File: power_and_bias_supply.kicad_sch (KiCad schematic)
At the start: 44 parts, among them Q501 2N7002, U501 MCP6L02x-xSN, U502 LM2733YMFX/NOPB, U503 TPS22944DCKR, X5 Conn_Coaxial

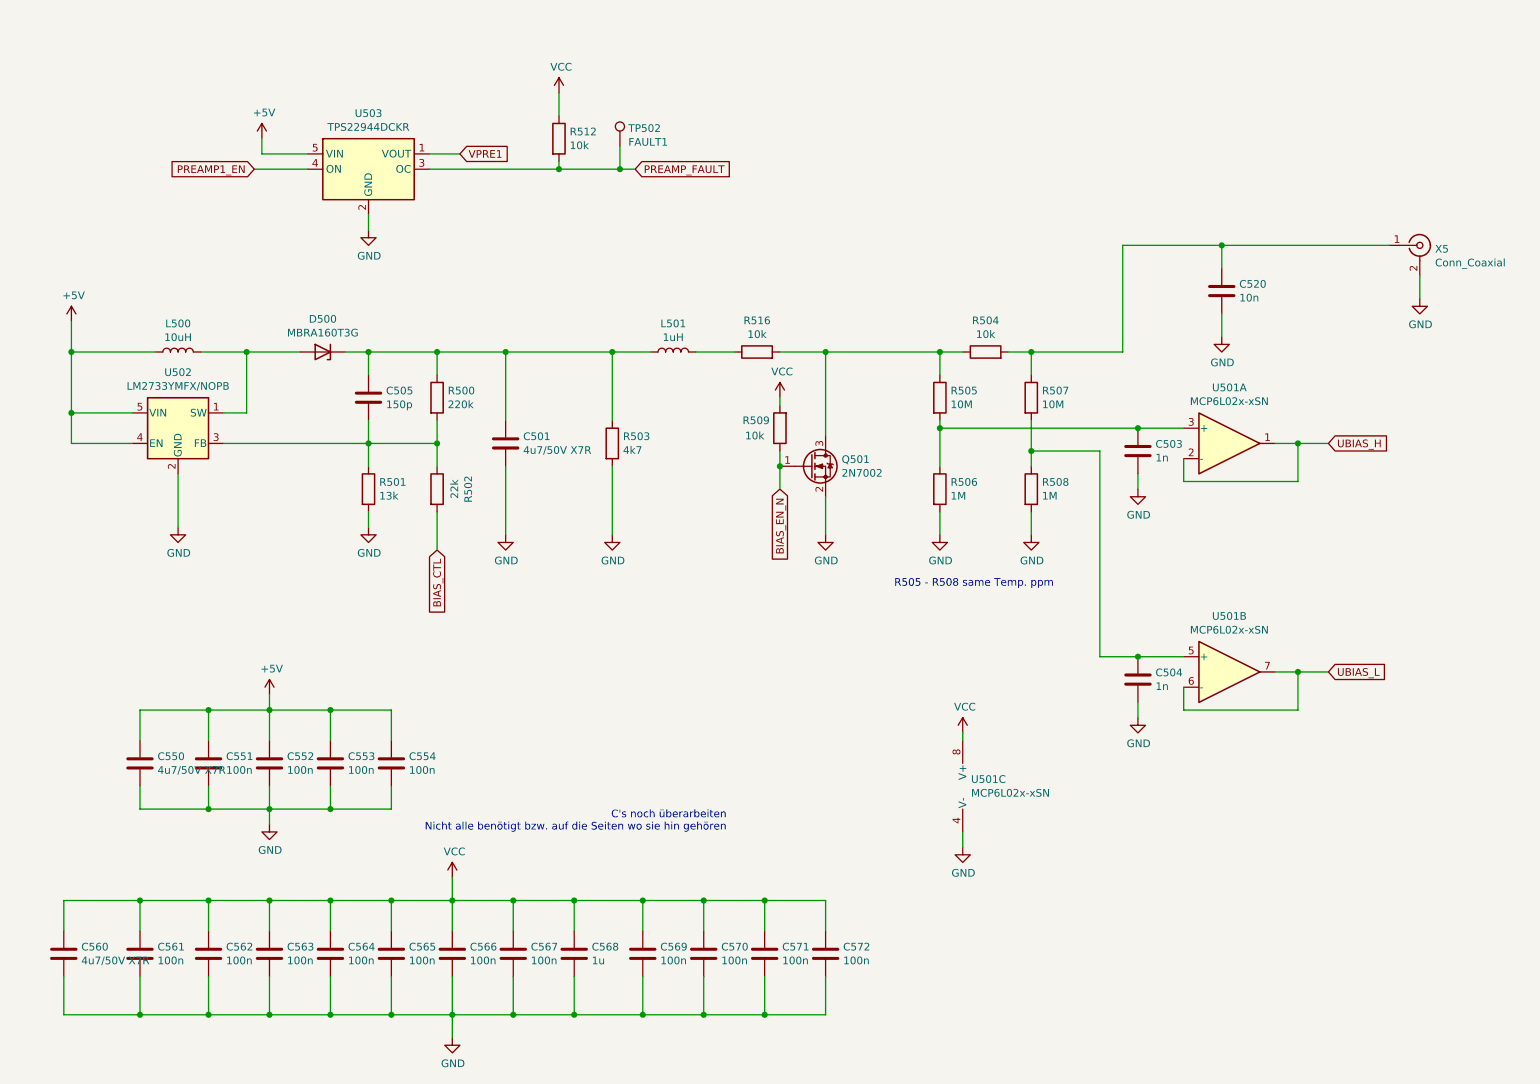
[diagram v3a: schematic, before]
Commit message: Footprints assigned. Testpoints added
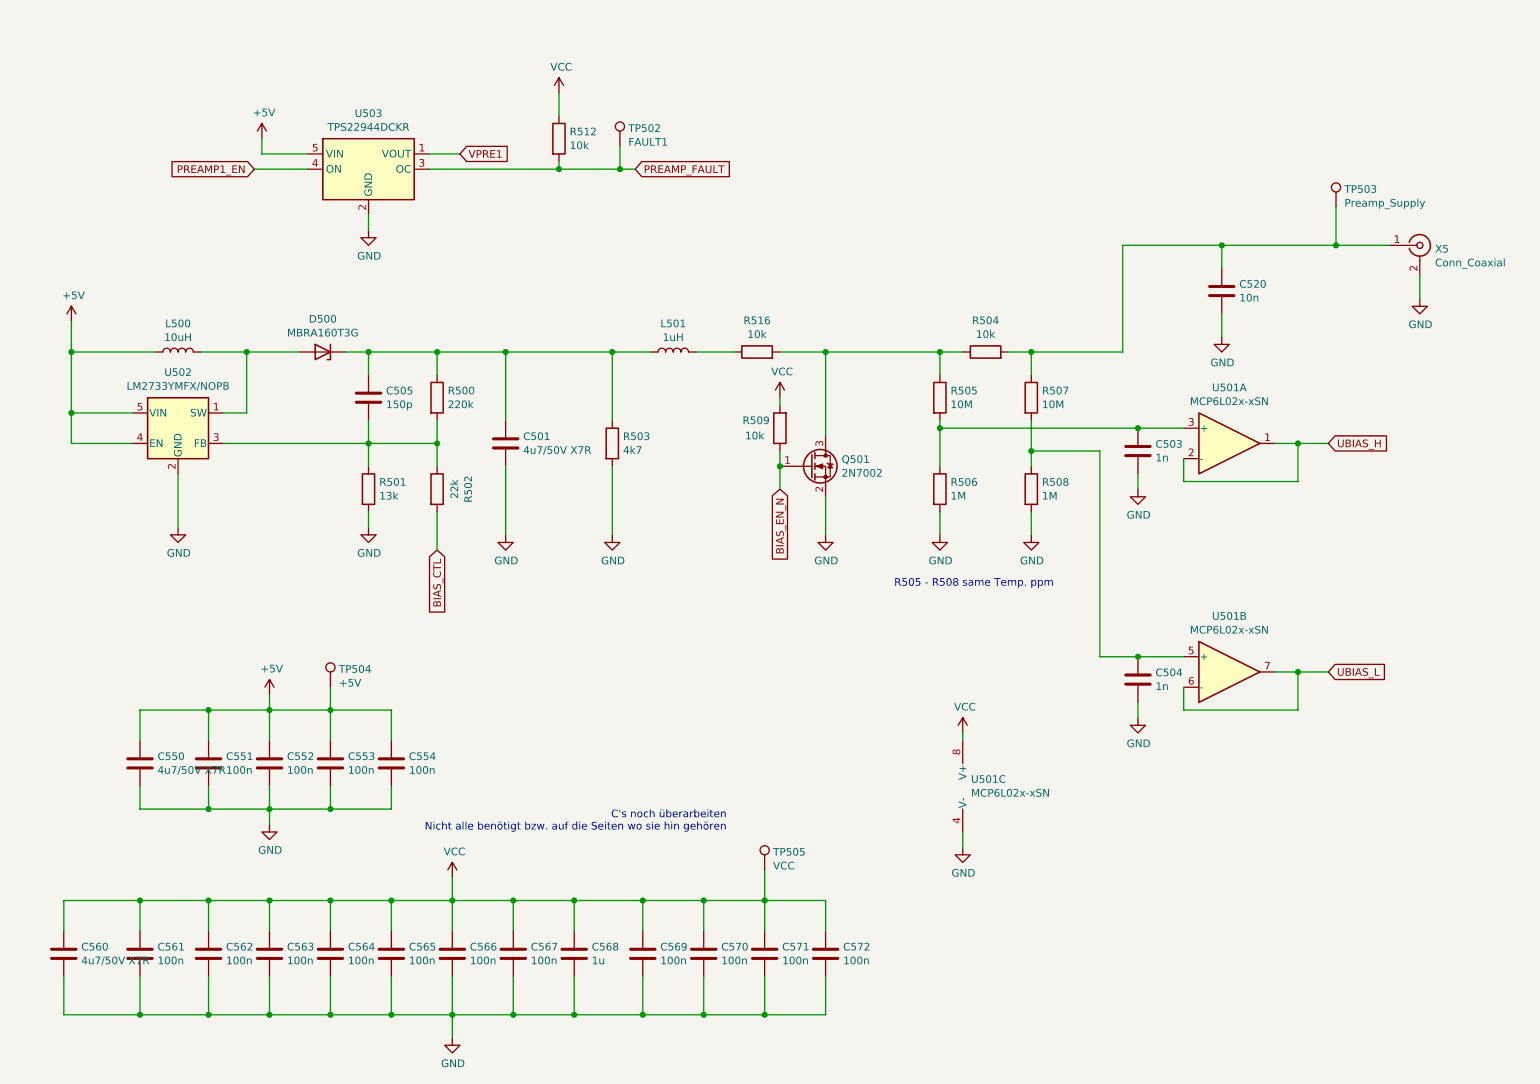
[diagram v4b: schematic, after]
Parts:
- added TP503: Preamp_Supply, TestPoint:TestPoint_THTPad_1.5x1.5mm_Drill0.7mm, symbol Connector:TestPoint
- added TP504: +5V, TestPoint:TestPoint_THTPad_1.5x1.5mm_Drill0.7mm, symbol Connector:TestPoint
- added TP505: VCC, TestPoint:TestPoint_THTPad_1.5x1.5mm_Drill0.7mm, symbol Connector:TestPoint
- TP502: footprint (none) -> TestPoint:TestPoint_THTPad_1.5x1.5mm_Drill0.7mm; now left out of the parts list
- U501: OriginalType (none) -> 579-MCP6L02T-E/SN; Supplier (none) -> Mouser
- U503: footprint (none) -> Package_TO_SOT_SMD:SOT-353_SC-70-5_Handsoldering; OriginalType (none) -> 595-TPS22944DCKR; Supplier (none) -> Mouser
- X5: footprint (none) -> muonpi-kicad-library:SMA_Samtec_SMA-J-P-X-ST-EM1_EdgeMount
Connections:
- net +5V: now also TP504.1
- net VCC: now also TP505.1
- net at C520.1, R504.2, R507.1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: now also TP503.1
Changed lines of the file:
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@@
   (junction (at 233.68 87.63) (diameter 1.016) (color 0 0 0 0))
   (junction (at 233.68 125.73) (diameter 1.016) (color 0 0 0 0))
+  (junction (at 240.03 54.61) (diameter 1.016) (color 0 0 0 0))
   (wire (pts (xy 27.94 163.83) (xy 27.94 168.91))
     (stroke (width 0) (type solid) (color 0 0 0 0))
@@
     (stroke (width 0) (type solid) (color 0 0 0 0))
   )
+  (wire (pts (xy 72.39 128.27) (xy 72.39 132.08))
+    (stroke (width 0) (type solid) (color 0 0 0 0))
+  )
   (wire (pts (xy 72.39 132.08) (xy 72.39 137.16))
     (stroke (width 0) (type solid) (color 0 0 0 0))
@@
     (stroke (width 0) (type solid) (color 0 0 0 0))
   )
+  (wire (pts (xy 144.78 158.75) (xy 144.78 163.83))
+    (stroke (width 0) (type solid) (color 0 0 0 0))
+  )
   (wire (pts (xy 144.78 163.83) (xy 134.62 163.83))
     (stroke (width 0) (type solid) (color 0 0 0 0))
@@
     (stroke (width 0) (type solid) (color 0 0 0 0))
   )
-  (wire (pts (xy 220.98 54.61) (xy 248.92 54.61))
+  (wire (pts (xy 220.98 54.61) (xy 240.03 54.61))
     (stroke (width 0) (type solid) (color 0 0 0 0))
   )
@@
   )
   (wire (pts (xy 233.68 132.08) (xy 233.68 125.73))
+    (stroke (width 0) (type solid) (color 0 0 0 0))
+  )
+  (wire (pts (xy 240.03 48.26) (xy 240.03 54.61))
+    (stroke (width 0) (type solid) (color 0 0 0 0))
+  )
+  (wire (pts (xy 240.03 54.61) (xy 248.92 54.61))
     (stroke (width 0) (type solid) (color 0 0 0 0))
   )
@@
     (pin "1")
   )
+  (symbol (lib_id "Connector:TestPoint") (at 72.39 128.27 0) (unit 1)
+    (in_bom no) (on_board yes)
+    (property "Reference" "TP504" (id 0) (at 73.7871 125.2791 0)
+      (effects (font (size 1.27 1.27)) (justify left))
+    )
+    (property "Value" "+5V" (id 1) (at 73.7871 127.5778 0)
+      (effects (font (size 1.27 1.27)) (justify left))
+    )
+    (property "Footprint" "TestPoint:TestPoint_THTPad_1.5x1.5mm_Drill0.7mm" (id 2) (at 77.47 128.27 0)
+      (effects (font (size 1.27 1.27)) hide)
+    )
+    (property "Datasheet" "~" (id 3) (at 77.47 128.27 0)
+      (effects (font (size 1.27 1.27)) hide)
+    )
+    (pin "1")
+  )
   (symbol (lib_id "Connector:TestPoint") (at 120.65 38.1 0) (unit 1)
-    (in_bom yes) (on_board yes)
+    (in_bom no) (on_board yes)
     (property "Reference" "TP502" (id 0) (at 122.0471 35.1091 0)
       (effects (font (size 1.27 1.27)) (justify left))
@@
       (effects (font (size 1.27 1.27)) (justify left))
     )
-    (property "Footprint" "" (id 2) (at 125.73 38.1 0)
+    (property "Footprint" "TestPoint:TestPoint_THTPad_1.5x1.5mm_Drill0.7mm" (id 2) (at 125.73 38.1 0)
       (effects (font (size 1.27 1.27)) hide)
     )
     (property "Datasheet" "~" (id 3) (at 125.73 38.1 0)
+      (effects (font (size 1.27 1.27)) hide)
+    )
+    (pin "1")
+  )
+  (symbol (lib_id "Connector:TestPoint") (at 144.78 158.75 0) (unit 1)
+    (in_bom no) (on_board yes)
+    (property "Reference" "TP505" (id 0) (at 146.1771 155.7591 0)
+      (effects (font (size 1.27 1.27)) (justify left))
+    )
+    (property "Value" "VCC" (id 1) (at 146.1771 158.0578 0)
+      (effects (font (size 1.27 1.27)) (justify left))
+    )
+    (property "Footprint" "TestPoint:TestPoint_THTPad_1.5x1.5mm_Drill0.7mm" (id 2) (at 149.86 158.75 0)
+      (effects (font (size 1.27 1.27)) hide)
+    )
+    (property "Datasheet" "~" (id 3) (at 149.86 158.75 0)
+      (effects (font (size 1.27 1.27)) hide)
+    )
+    (pin "1")
+  )
+  (symbol (lib_id "Connector:TestPoint") (at 240.03 48.26 0) (unit 1)
+    (in_bom no) (on_board yes)
+    (property "Reference" "TP503" (id 0) (at 241.4271 45.2691 0)
+      (effects (font (size 1.27 1.27)) (justify left))
+    )
+    (property "Value" "Preamp_Supply" (id 1) (at 241.4271 47.5678 0)
+      (effects (font (size 1.27 1.27)) (justify left))
+    )
+    (property "Footprint" "TestPoint:TestPoint_THTPad_1.5x1.5mm_Drill0.7mm" (id 2) (at 245.11 48.26 0)
+      (effects (font (size 1.27 1.27)) hide)
+    )
+    (property "Datasheet" "~" (id 3) (at 245.11 48.26 0)
       (effects (font (size 1.27 1.27)) hide)
     )
@@
       (effects (font (size 1.27 1.27)) hide)
     )
-    (property "Datasheet" "http://ww1.microchip.com/downloads/en/devicedoc/22140b.pdf" (id 3) (at 184.15 140.97 0)
+    (property "Datasheet" "~" (id 3) (at 184.15 140.97 0)
+      (effects (font (size 1.27 1.27)) hide)
+    )
+    (property "OriginalType" "579-MCP6L02T-E/SN" (id 4) (at 177.8 144.78 0)
+      (effects (font (size 1.27 1.27)) hide)
+    )
+    (property "Supplier" "Mouser" (id 5) (at 177.8 144.78 0)
       (effects (font (size 1.27 1.27)) hide)
     )
@@
       (effects (font (size 1.27 1.27)) (justify left))
     )
-    (property "Footprint" "" (id 2) (at 254 54.61 0)
+    (property "Footprint" "muonpi-kicad-library:SMA_Samtec_SMA-J-P-X-ST-EM1_EdgeMount" (id 2) (at 254 54.61 0)
       (effects (font (size 1.27 1.27)) hide)
     )
@@
     (pin "3")
   )
-  (symbol (lib_name "Amplifier_Operational:MCP6L02x-xSN_2") (lib_id "Amplifier_Operational:MCP6L02x-xSN") (at 222.25 87.63 0) (unit 1)
+  (symbol (lib_id "Amplifier_Operational:MCP6L02x-xSN") (at 222.25 87.63 0) (unit 1)
     (in_bom yes) (on_board yes)
     (property "Reference" "U501" (id 0) (at 222.25 78.3398 0))
@@
       (effects (font (size 1.27 1.27)) hide)
     )
-    (property "Datasheet" "http://ww1.microchip.com/downloads/en/devicedoc/22140b.pdf" (id 3) (at 228.6 83.82 0)
+    (property "Datasheet" "~" (id 3) (at 228.6 83.82 0)
+      (effects (font (size 1.27 1.27)) hide)
+    )
+    (property "OriginalType" "579-MCP6L02T-E/SN" (id 4) (at 222.25 87.63 0)
+      (effects (font (size 1.27 1.27)) hide)
+    )
+    (property "Supplier" "Mouser" (id 5) (at 222.25 87.63 0)
       (effects (font (size 1.27 1.27)) hide)
     )
@@
     (pin "3")
   )
-  (symbol (lib_name "Amplifier_Operational:MCP6L02x-xSN_1") (lib_id "Amplifier_Operational:MCP6L02x-xSN") (at 222.25 125.73 0) (unit 2)
+  (symbol (lib_id "Amplifier_Operational:MCP6L02x-xSN") (at 222.25 125.73 0) (unit 2)
     (in_bom yes) (on_board yes)
     (property "Reference" "U501" (id 0) (at 222.25 116.4398 0))
@@
     )
     (property "Datasheet" "http://ww1.microchip.com/downloads/en/devicedoc/22140b.pdf" (id 3) (at 228.6 121.92 0)
+      (effects (font (size 1.27 1.27)) hide)
+    )
+    (property "OriginalType" "579-MCP6L02T-E/SN" (id 4) (at 222.25 125.73 0)
+      (effects (font (size 1.27 1.27)) hide)
+    )
+    (property "Supplier" "Mouser" (id 5) (at 222.25 125.73 0)
       (effects (font (size 1.27 1.27)) hide)
     )
@@
     (property "Reference" "U503" (id 0) (at 78.74 32.6198 0))
     (property "Value" "TPS22944DCKR" (id 1) (at 78.74 34.9185 0))
-    (property "Footprint" "" (id 2) (at 78.74 29.21 0)
+    (property "Footprint" "Package_TO_SOT_SMD:SOT-353_SC-70-5_Handsoldering" (id 2) (at 78.74 29.21 0)
       (effects (font (size 1.27 1.27)) hide)
     )
@@
       (effects (font (size 1.27 1.27)) hide)
     )
+    (property "OriginalType" "595-TPS22944DCKR " (id 4) (at 78.74 41.91 0)
+      (effects (font (size 1.27 1.27)) hide)
+    )
+    (property "Supplier" "Mouser" (id 5) (at 78.74 41.91 0)
+      (effects (font (size 1.27 1.27)) hide)
+    )

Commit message: Changed the position of the capacitor in the circuit diagram. Capacitors are now close to the components as on the circuit board.
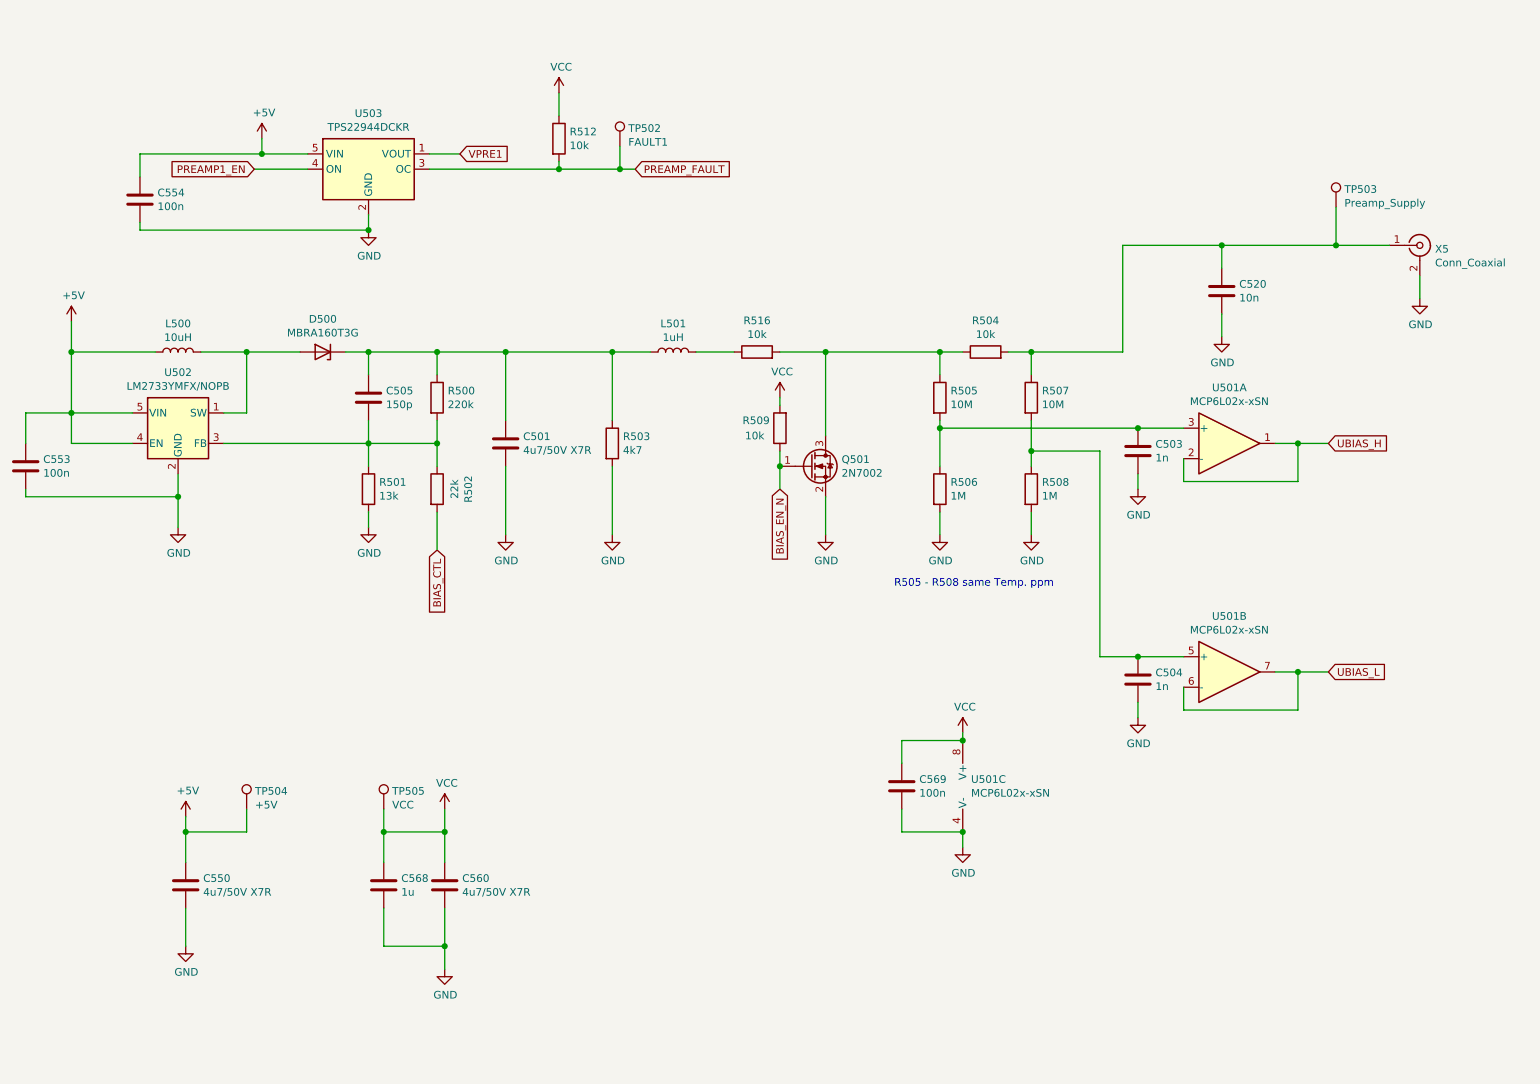
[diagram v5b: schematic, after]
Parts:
- removed C551, C552, C561, C562, C563, C564, C565, C566, C567, C570, C571, C572: 100n, Capacitor_SMD:C_0805_2012Metric_Pad1.18x1.45mm_HandSolder, symbol Device:C
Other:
- note removed: "C's noch überarbeiten Nicht alle benötigt bzw. auf die Seiten wo sie hin gehören"
- moved on the sheet: C550, C553, C554, C560, C568, C569, TP504, TP505
